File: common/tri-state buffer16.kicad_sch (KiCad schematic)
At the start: 5 parts, among them IC3 SN74AHCT16245ADGGR

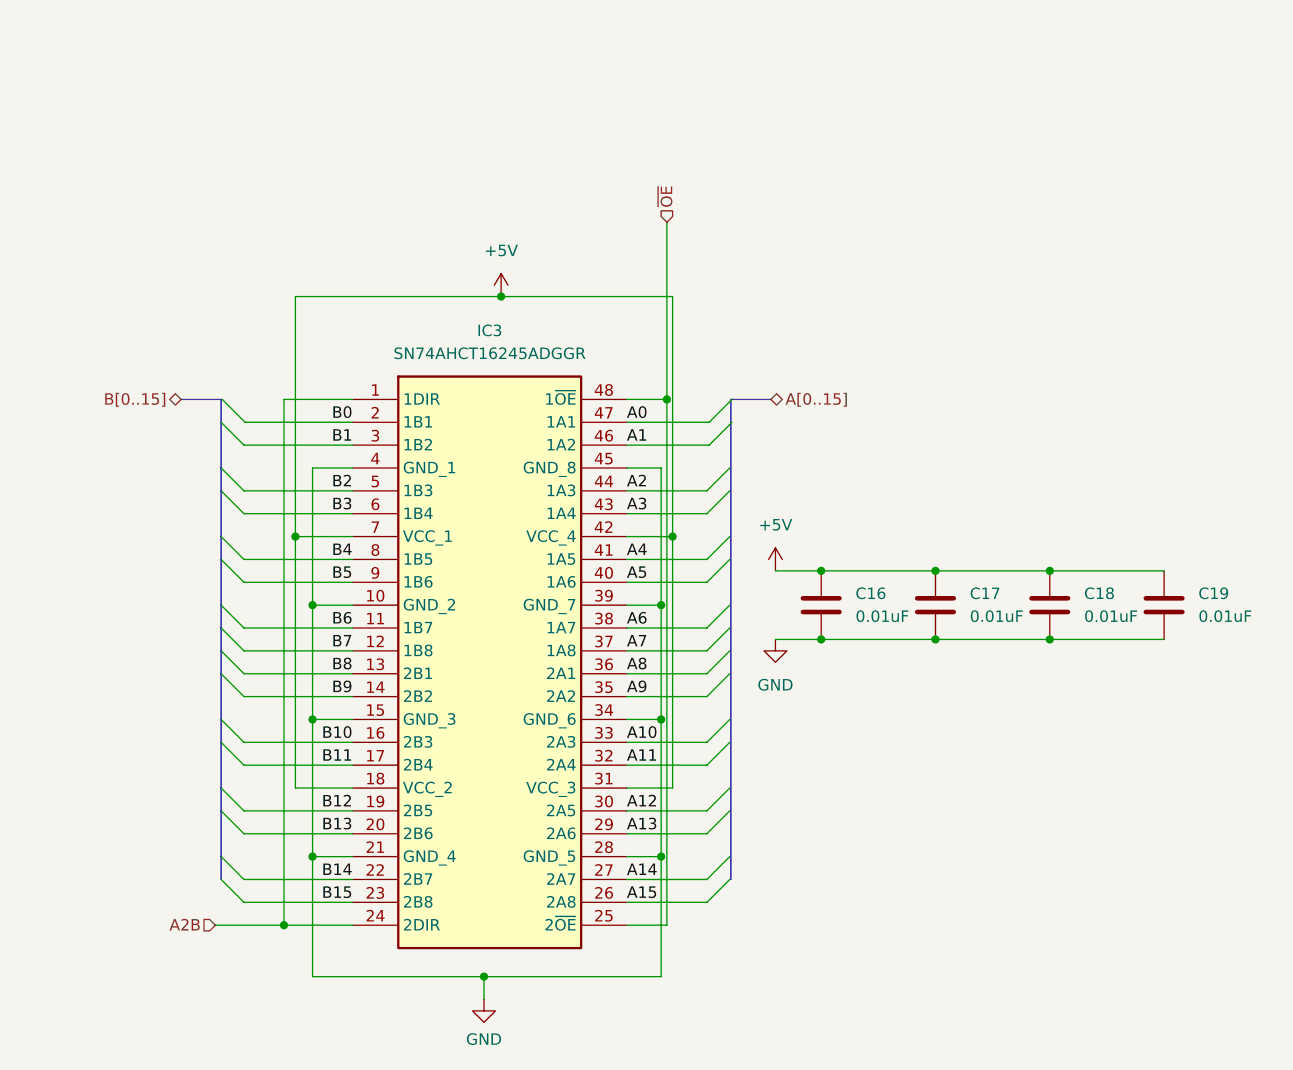
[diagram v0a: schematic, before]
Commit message: Updated ALU and moved common schematics to common/ for enhanced reusability
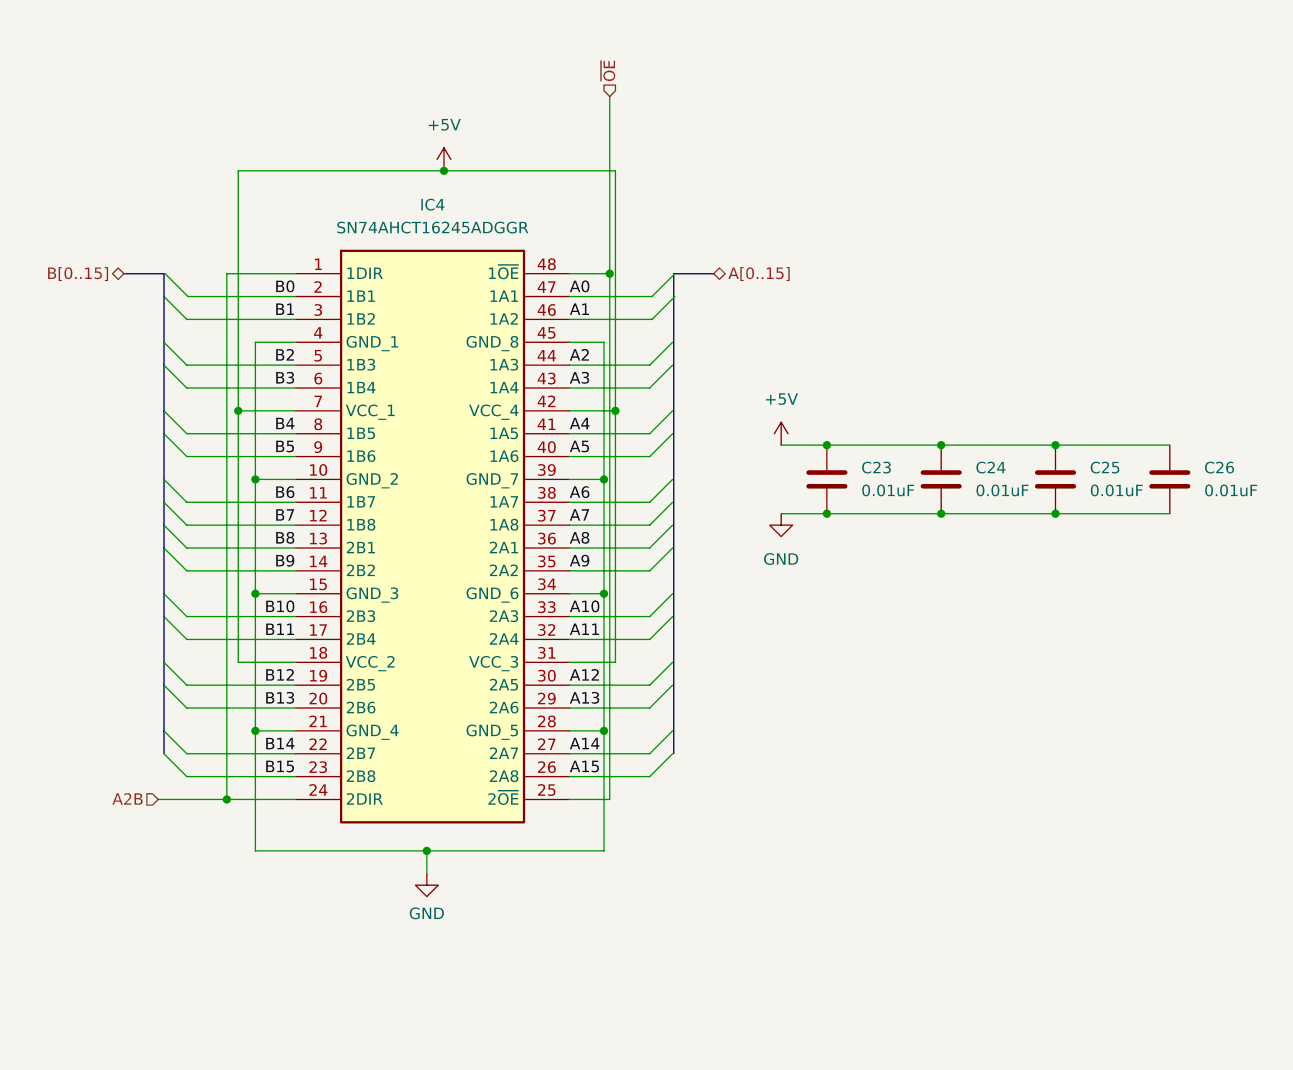
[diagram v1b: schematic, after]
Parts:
- renumbered C16 to C23, C17 to C24, C18 to C25, C19 to C26, IC3 to IC4
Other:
- title: (none) -> 16-Bit Bidirectional Tri-State Buffer
- moved on the sheet: C23, C24, C25, C26, IC4

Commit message: Fixed tri-state buffer and completed double buffer PCB
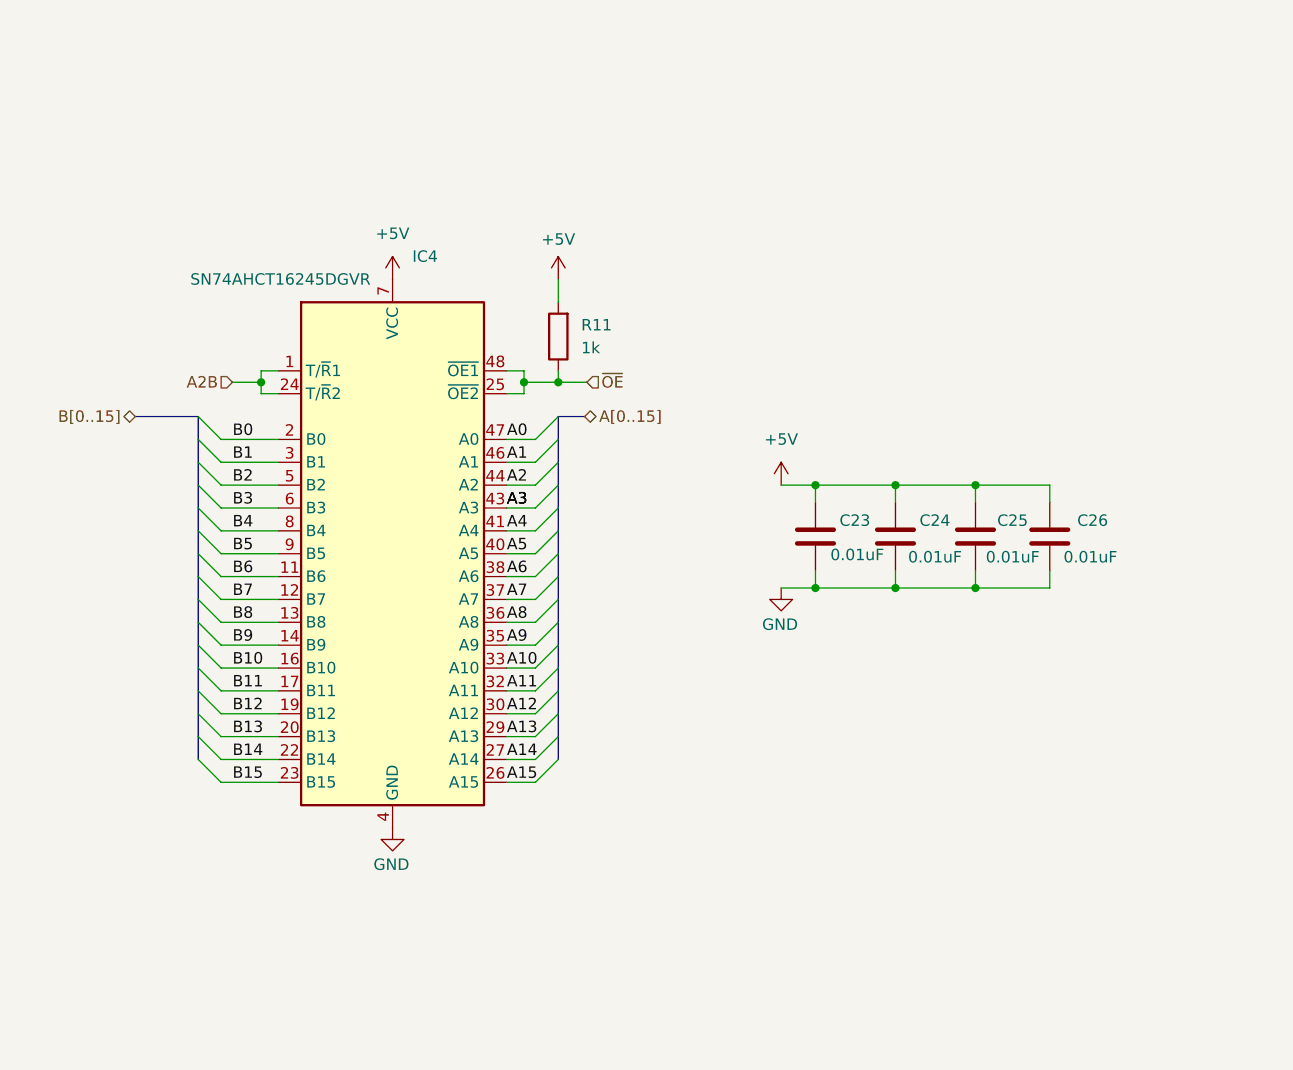
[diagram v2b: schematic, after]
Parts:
- removed IC4: SN74AHCT16245ADGGR, Package_SO:TSSOP-48_6.1x12.5mm_P0.5mm, symbol SN74LVC16245ADGVR:SN74LVC16245ADGVR
- added IC4: SN74AHCT16245DGVR, Package_SO:TSSOP-48_6.1x12.5mm_P0.5mm, symbol 74xx:MC74LCX16245DT
- added R11: 1k, Resistor_SMD:R_0603_1608Metric, symbol Device:R
- C23, C24, C25, C26: Manufacturer_Part_Number CL10B104KO8WPNL -> (none)
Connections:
- net +5V: now also IC4.18 (VCC), IC4.31 (VCC), IC4.42 (VCC), IC4.7 (VCC), R11.2
- net A0: now also IC4.47 (A0)
- net A1: now also IC4.46 (A1)
- net A10: now also IC4.33 (A10)
- net A11: now also IC4.32 (A11)
- net A12: now also IC4.30 (A12)
- net A13: now also IC4.29 (A13)
- net A14: now also IC4.27 (A14)
- net A15: now also IC4.26 (A15)
- net A2: now also IC4.44 (A2)
- net A2B: now also IC4.1 (T/~{R}1), IC4.24 (T/~{R}2)
- net A3: now also IC4.43 (A3)
- net A4: now also IC4.41 (A4)
- net A5: now also IC4.40 (A5)
- net A6: now also IC4.38 (A6)
- net A7: now also IC4.37 (A7)
- net A8: now also IC4.36 (A8)
- net A9: now also IC4.35 (A9)
- net B0: now also IC4.2 (B0)
- net B1: now also IC4.3 (B1)
- net B10: now also IC4.16 (B10)
- net B11: now also IC4.17 (B11)
- net B12: now also IC4.19 (B12)
- net B13: now also IC4.20 (B13)
- net B14: now also IC4.22 (B14)
- net B15: now also IC4.23 (B15)
- net B2: now also IC4.5 (B2)
- net B3: now also IC4.6 (B3)
- net B4: now also IC4.8 (B4)
- net B5: now also IC4.9 (B5)
- net B6: now also IC4.11 (B6)
- net B7: now also IC4.12 (B7)
- net B8: now also IC4.13 (B8)
- net B9: now also IC4.14 (B9)
- net GND: now also IC4.10 (GND), IC4.15 (GND), IC4.21 (GND), IC4.28 (GND), IC4.34 (GND), IC4.39 (GND), IC4.4 (GND), IC4.45 (GND)
- net ~{OE}: now also IC4.25 (~{OE2}), IC4.48 (~{OE1}), R11.1

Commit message: Made tri-state and register schematic look nice
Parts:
- IC4: value SN74AHCT16245DGVR -> SN74AHCT16245DGGR
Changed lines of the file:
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@@
 			)
 		)
-		(property "Value" "SN74AHCT16245DGVR"
+		(property "Value" "SN74AHCT16245DGGR"
 			(at 34.036 38.735 0)
 			(effects

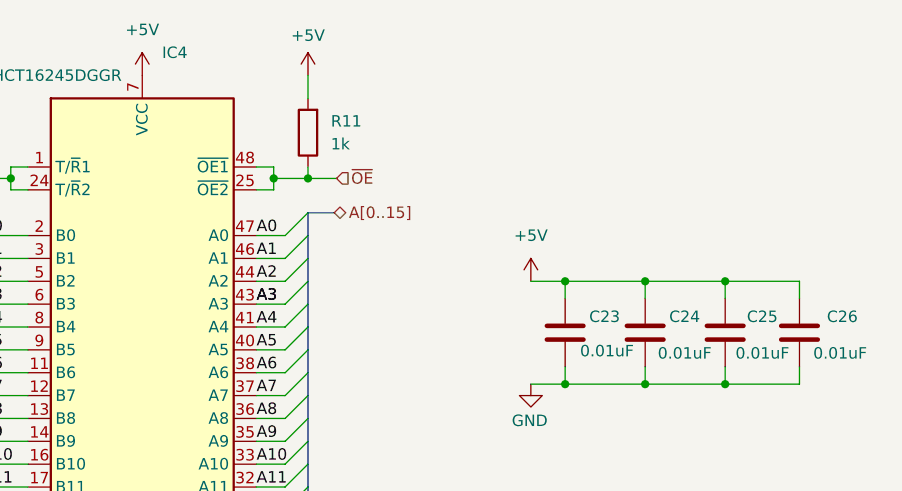
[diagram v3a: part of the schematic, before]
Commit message: Fixed incorrect wiring in ALU (input registers)
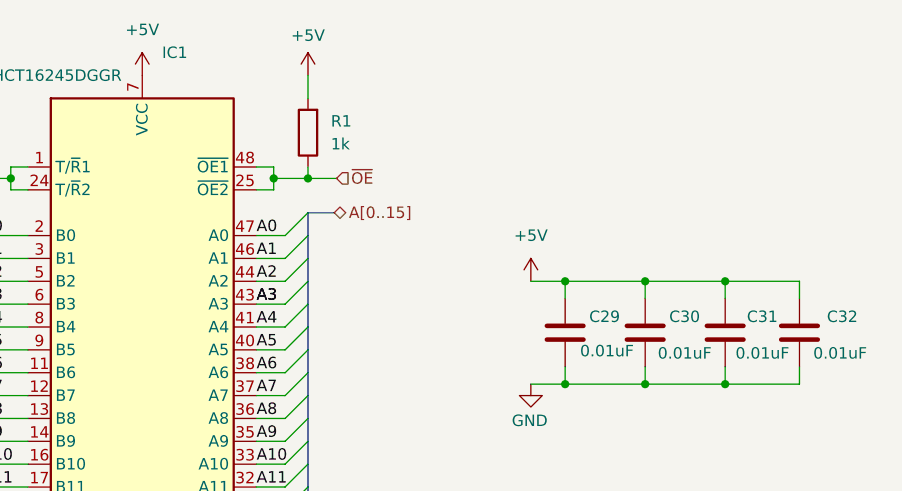
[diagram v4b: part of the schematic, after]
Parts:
- renumbered C23 to C29, C24 to C30, C25 to C31, C26 to C32, IC4 to IC1, R11 to R1
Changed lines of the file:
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@@
 (kicad_sch
-	(version 20231120)
+	(version 20250114)
 	(generator "eeschema")
-	(generator_version "8.0")
+	(generator_version "9.0")
 	(paper "A4")
 	(title_block
 		(title "16-Bit Bidirectional Tri-State Buffer")
-		(rev "V1.0")
+		(rev "V1.1")
 	)
 	(junction
@@
 	(label "A0"
 		(at 69.215 56.515 0)
-		(fields_autoplaced yes)
 		(effects
 			(font
@@
 	(label "B5"
 		(at 38.735 69.215 0)
-		(fields_autoplaced yes)
 		(effects
 			(font
@@
 	(label "B10"
 		(at 38.735 81.915 0)
-		(fields_autoplaced yes)
 		(effects
 			(font
@@
 	(label "A15"
 		(at 69.215 94.615 0)
-		(fields_autoplaced yes)
 		(effects
 			(font
@@
 	(label "A7"
 		(at 69.215 74.295 0)
-		(fields_autoplaced yes)
 		(effects
 			(font
@@
 	(label "A4"
 		(at 69.215 66.675 0)
-		(fields_autoplaced yes)
 		(effects
 			(font
@@
 	(label "A12"
 		(at 69.215 86.995 0)
-		(fields_autoplaced yes)
 		(effects
 			(font
@@
 	(label "A9"
 		(at 69.215 79.375 0)
-		(fields_autoplaced yes)
 		(effects
 			(font
@@
 	(label "B0"
 		(at 38.735 56.515 0)
-		(fields_autoplaced yes)
 		(effects
 			(font
@@
 	(label "B2"
 		(at 38.735 61.595 0)
-		(fields_autoplaced yes)
 		(effects
 			(font
@@
 	(label "A2"
 		(at 69.215 61.595 0)
-		(fields_autoplaced yes)
 		(effects
 			(font
@@
 	(label "B12"
 		(at 38.735 86.995 0)
-		(fields_autoplaced yes)
 		(effects
 			(font
@@
 	(label "B9"
 		(at 38.735 79.375 0)
-		(fields_autoplaced yes)
 		(effects
 			(font
@@
 	(label "A11"
 		(at 69.215 84.455 0)
-		(fields_autoplaced yes)
 		(effects
 			(font
@@
 	(label "B3"
 		(at 38.735 64.135 0)
-		(fields_autoplaced yes)
 		(effects
 			(font
@@
 	(label "B4"
 		(at 38.735 66.675 0)
-		(fields_autoplaced yes)
 		(effects
 			(font
@@
 	(label "A3"
 		(at 69.215 64.135 0)
-		(fields_autoplaced yes)
 		(effects
 			(font
@@
 	(label "A13"
 		(at 69.215 89.535 0)
-		(fields_autoplaced yes)
 		(effects
 			(font
@@
 	(label "A6"
 		(at 69.215 71.755 0)
-		(fields_autoplaced yes)
 		(effects
 			(font
@@
 	(label "A1"
 		(at 69.215 59.055 0)
-		(fields_autoplaced yes)
 		(effects
 			(font
@@
 	(label "B1"
 		(at 38.735 59.055 0)
-		(fields_autoplaced yes)
 		(effects
 			(font
@@
 	(label "A8"
 		(at 69.215 76.835 0)
-		(fields_autoplaced yes)
 		(effects
 			(font
@@
 	(label "B7"
 		(at 38.735 74.295 0)
-		(fields_autoplaced yes)
 		(effects
 			(font
@@
 	(label "B11"
 		(at 38.735 84.455 0)
-		(fields_autoplaced yes)
 		(effects
 			(font
@@
 	(label "A14"
 		(at 69.215 92.075 0)
-		(fields_autoplaced yes)
 		(effects
 			(font
@@
 	(label "B15"
 		(at 38.735 94.615 0)
-		(fields_autoplaced yes)
 		(effects
 			(font
@@
 	(label "B14"
 		(at 38.735 92.075 0)
-		(fields_autoplaced yes)
 		(effects
 			(font
@@
 	(label "A3"
 		(at 69.215 64.135 0)
-		(fields_autoplaced yes)
 		(effects
 			(font
@@
 	(label "A5"
 		(at 69.215 69.215 0)
-		(fields_autoplaced yes)
 		(effects
 			(font
@@
 	(label "B6"
 		(at 38.735 71.755 0)
-		(fields_autoplaced yes)
 		(effects
 			(font
@@
 	(label "B13"
 		(at 38.735 89.535 0)
-		(fields_autoplaced yes)
 		(effects
 			(font
@@
 	(label "A10"
 		(at 69.215 81.915 0)
-		(fields_autoplaced yes)
 		(effects
 			(font
@@
 	(label "B8"
 		(at 38.735 76.835 0)
-		(fields_autoplaced yes)
 		(effects
 			(font
@@
 		(shape input)
 		(at 38.735 50.165 180)
-		(fields_autoplaced yes)
 		(effects
 			(font
@@
 		(shape input)
 		(at 78.105 50.165 0)
-		(fields_autoplaced yes)
 		(effects
 			(font
@@
 		(shape bidirectional)
 		(at 77.851 53.975 0)
-		(fields_autoplaced yes)
 		(effects
 			(font
@@
 		(shape bidirectional)
 		(at 27.94 53.975 180)
-		(fields_autoplaced yes)
 		(effects
 			(font
@@
 		(on_board yes)
 		(dnp no)
-		(property "Reference" "#PWR055"
+		(property "Reference" "#PWR0102"
 			(at 56.515 106.045 0)
 			(effects
@@
 		(on_board yes)
 		(dnp no)
-		(property "Reference" "IC4"
+		(property "Reference" "IC1"
 			(at 58.7091 36.195 0)
 			(effects
@@
 		(dnp no)
 		(fields_autoplaced yes)
-		(property "Reference" "#PWR051"
+		(property "Reference" "#PWR0103"
 			(at 56.515 42.545 0)
 			(effects
@@
 		(on_board yes)
 		(dnp no)
-		(property "Reference" "#PWR031"
+		(property "Reference" "#PWR0101"
 			(at 99.695 79.375 0)
 			(effects
@@
 		(on_board yes)
 		(dnp no)
-		(property "Reference" "C26"
+		(property "Reference" "C32"
 			(at 132.588 65.532 0)
 			(effects
@@
 		(on_board yes)
 		(dnp no)
-		(property "Reference" "C23"
+		(property "Reference" "C29"
 			(at 106.172 65.532 0)
 			(effects
@@
 		(dnp no)
 		(fields_autoplaced yes)
-		(property "Reference" "#PWR047"
+		(property "Reference" "#PWR0104"
 			(at 74.93 42.545 0)
 			(effects
@@
 		(on_board yes)
 		(dnp no)
-		(property "Reference" "C25"
+		(property "Reference" "C31"
 			(at 123.698 65.532 0)
 			(effects
@@
 		(dnp no)
 		(fields_autoplaced yes)
-		(property "Reference" "#PWR027"
+		(property "Reference" "#PWR0105"
 			(at 99.695 65.405 0)
 			(effects
@@
 		(on_board yes)
 		(dnp no)
-		(property "Reference" "C24"
+		(property "Reference" "C30"
 			(at 115.062 65.532 0)
 			(effects
@@
 		(dnp no)
 		(fields_autoplaced yes)
-		(property "Reference" "R11"
+		(property "Reference" "R1"
 			(at 77.47 43.8149 0)
 			(effects

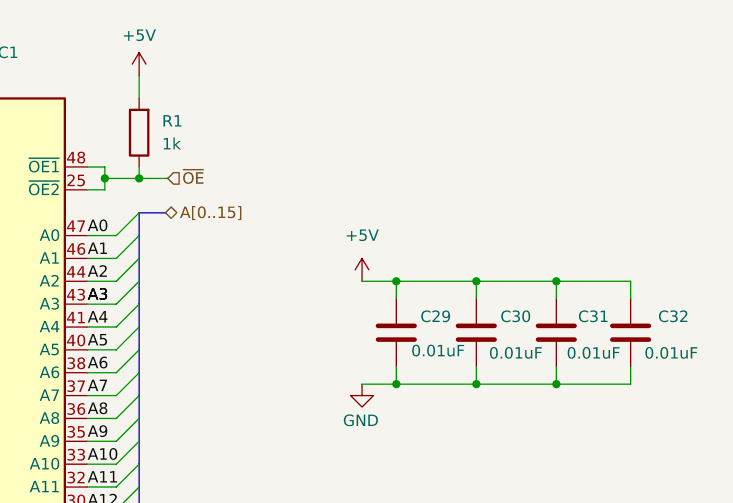
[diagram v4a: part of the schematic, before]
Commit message: Refactored files, finalized reg4x16, and used lowercase v
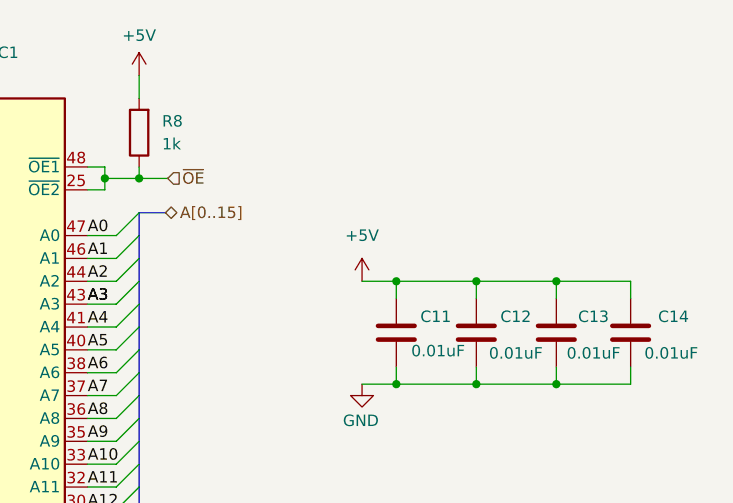
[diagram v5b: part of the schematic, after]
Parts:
- renumbered C29 to C11, C30 to C12, C31 to C13, C32 to C14, R1 to R8
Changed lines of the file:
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@@
 		(on_board yes)
 		(dnp no)
-		(property "Reference" "#PWR0102"
+		(property "Reference" "#PWR052"
 			(at 56.515 106.045 0)
 			(effects
@@
 		(dnp no)
 		(fields_autoplaced yes)
-		(property "Reference" "#PWR0103"
+		(property "Reference" "#PWR048"
 			(at 56.515 42.545 0)
 			(effects
@@
 		(on_board yes)
 		(dnp no)
-		(property "Reference" "#PWR0101"
+		(property "Reference" "#PWR028"
 			(at 99.695 79.375 0)
 			(effects
@@
 		(on_board yes)
 		(dnp no)
-		(property "Reference" "C32"
+		(property "Reference" "C14"
 			(at 132.588 65.532 0)
 			(effects
@@
 		(on_board yes)
 		(dnp no)
-		(property "Reference" "C29"
+		(property "Reference" "C11"
 			(at 106.172 65.532 0)
 			(effects
@@
 		(dnp no)
 		(fields_autoplaced yes)
-		(property "Reference" "#PWR0104"
+		(property "Reference" "#PWR044"
 			(at 74.93 42.545 0)
 			(effects
@@
 		(on_board yes)
 		(dnp no)
-		(property "Reference" "C31"
+		(property "Reference" "C13"
 			(at 123.698 65.532 0)
 			(effects
@@
 		(dnp no)
 		(fields_autoplaced yes)
-		(property "Reference" "#PWR0105"
+		(property "Reference" "#PWR024"
 			(at 99.695 65.405 0)
 			(effects
@@
 		(on_board yes)
 		(dnp no)
-		(property "Reference" "C30"
+		(property "Reference" "C12"
 			(at 115.062 65.532 0)
 			(effects
@@
 		(dnp no)
 		(fields_autoplaced yes)
-		(property "Reference" "R1"
+		(property "Reference" "R8"
 			(at 77.47 43.8149 0)
 			(effects

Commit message: Memory Controller- Initial setup
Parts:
- renumbered C11 to C29, C12 to C30, C13 to C31, C14 to C32, R8 to R1
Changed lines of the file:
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@@
 		(on_board yes)
 		(dnp no)
-		(property "Reference" "#PWR052"
+		(property "Reference" "#PWR0102"
 			(at 56.515 106.045 0)
 			(effects
@@
 		(dnp no)
 		(fields_autoplaced yes)
-		(property "Reference" "#PWR048"
+		(property "Reference" "#PWR0103"
 			(at 56.515 42.545 0)
 			(effects
@@
 		(on_board yes)
 		(dnp no)
-		(property "Reference" "#PWR028"
+		(property "Reference" "#PWR0101"
 			(at 99.695 79.375 0)
 			(effects
@@
 		(on_board yes)
 		(dnp no)
-		(property "Reference" "C14"
+		(property "Reference" "C32"
 			(at 132.588 65.532 0)
 			(effects
@@
 		(on_board yes)
 		(dnp no)
-		(property "Reference" "C11"
+		(property "Reference" "C29"
 			(at 106.172 65.532 0)
 			(effects
@@
 		(dnp no)
 		(fields_autoplaced yes)
-		(property "Reference" "#PWR044"
+		(property "Reference" "#PWR0104"
 			(at 74.93 42.545 0)
 			(effects
@@
 		(on_board yes)
 		(dnp no)
-		(property "Reference" "C13"
+		(property "Reference" "C31"
 			(at 123.698 65.532 0)
 			(effects
@@
 		(dnp no)
 		(fields_autoplaced yes)
-		(property "Reference" "#PWR024"
+		(property "Reference" "#PWR0105"
 			(at 99.695 65.405 0)
 			(effects
@@
 		(on_board yes)
 		(dnp no)
-		(property "Reference" "C12"
+		(property "Reference" "C30"
 			(at 115.062 65.532 0)
 			(effects
@@
 		(dnp no)
 		(fields_autoplaced yes)
-		(property "Reference" "R8"
+		(property "Reference" "R1"
 			(at 77.47 43.8149 0)
 			(effects
